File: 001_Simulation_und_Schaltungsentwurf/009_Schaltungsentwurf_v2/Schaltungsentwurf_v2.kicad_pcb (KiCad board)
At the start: 4 copper layers, 146 x 82.1 mm, 101 parts, among them IC1 MPY634KP, IC2 MPY634KP, IC3 MPY634KP, J1 Screw_Terminal_01x04, J2 Conn_Coaxial, J3 Conn_Coaxial, J4 Conn_Coaxial, J5 Conn_Coaxial, J6 Conn_Coaxial, SW1 SW_MEC_5G, U1 TL082, U2 TL082, U3 MCP4261-104E_P, U4 MCP4261-104E_P, U5 TL082, U6 LM2596T-3.3

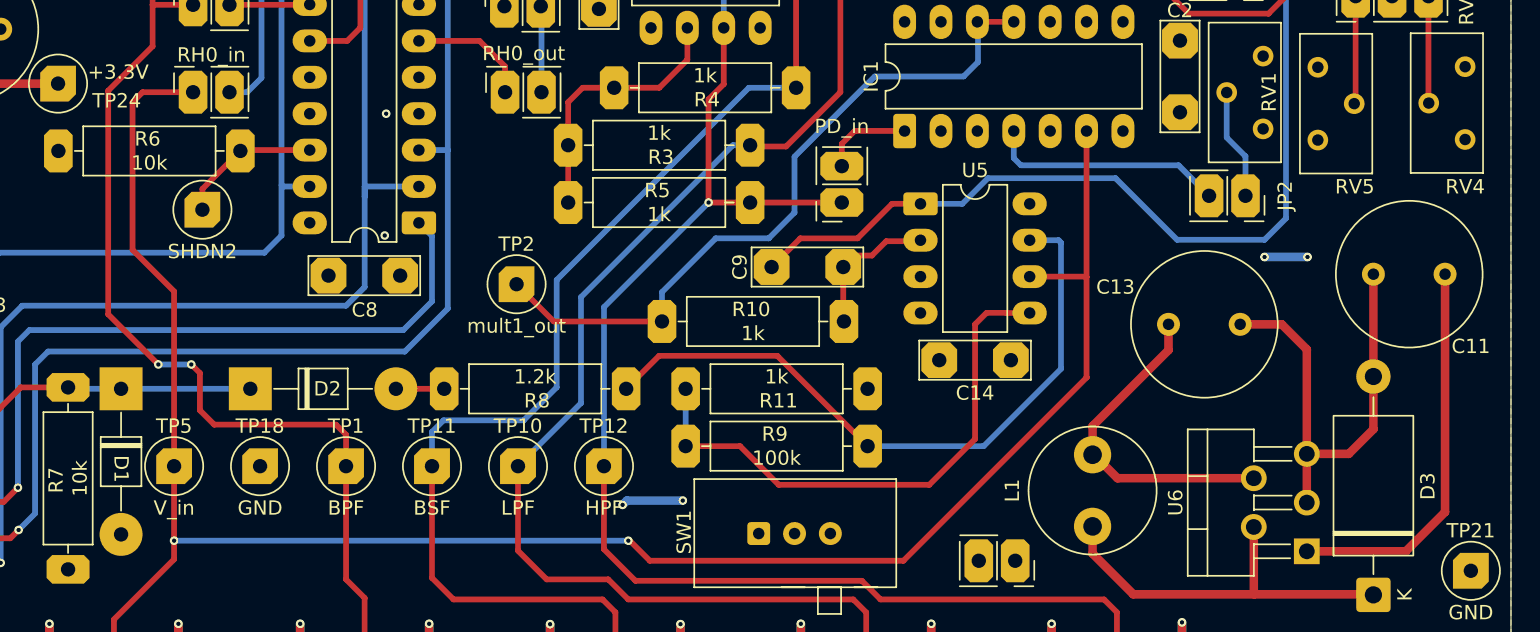
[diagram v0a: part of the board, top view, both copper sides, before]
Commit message: PD-Vermessung und Sprungantwortsimulation
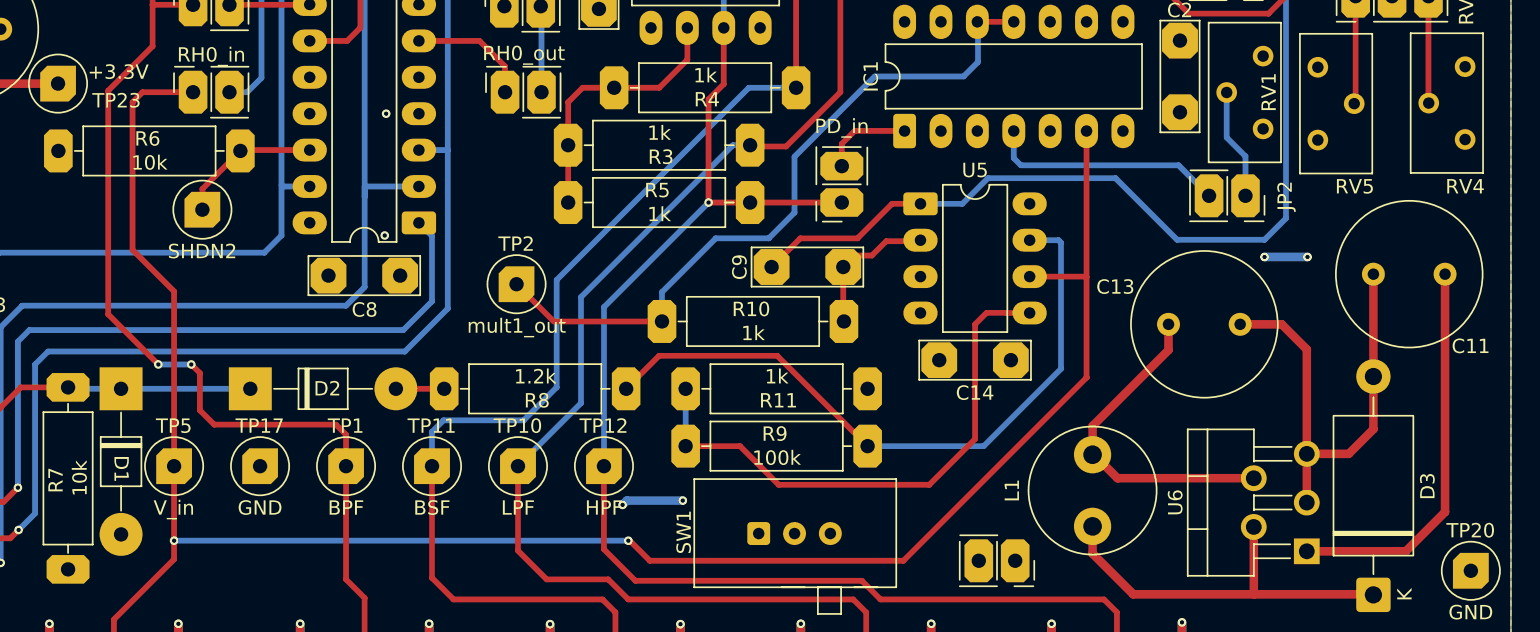
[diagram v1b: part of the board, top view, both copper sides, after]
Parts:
- renumbered JP17 to JP16, JP18 to JP17, JP19 to JP18, TP16 to TP15, TP17 to TP16, TP18 to TP17, TP19 to TP18, TP20 to TP19, TP21 to TP20, TP22 to TP21, TP23 to TP22, TP24 to TP23
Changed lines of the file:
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@@
 	(net 89 "unconnected-(U4-P0B-Pad10)")
 	(net 90 "HPF_in")
-	(net 91 "Net-(JP19-A)")
+	(net 91 "Net-(JP16-A)")
 	(net 92 "Net-(D1-K)")
 	(net 93 "Net-(D2-A)")
@@
 	(net 95 "Net-(JP17-A)")
 	(net 96 "Net-(JP18-A)")
-	(net 97 "Net-(JP19-B)")
+	(net 97 "Net-(JP18-B)")
 	(net 98 "Net-(R8-Pad1)")
 	(footprint "000_OUF:TestPoint"
@@
 				(keep_text_aligned yes)
 			)
-			(gr_text "0,1673 in"
+			(gr_text "4,2500 mm"
 				(at 189.775 123.55 0)
 				(layer "User.2")
@@
 				(keep_text_aligned yes)
 			)
-			(gr_text "0,1673 in"
+			(gr_text "4,2500 mm"
 				(at 194.025 123.548 0)
 				(layer "User.2")
@@
 		(descr "THT pad as test Point, diameter 2.0mm, hole diameter 1.0mm")
 		(tags "test point THT pad")
-		(property "Reference" "TP23"
+		(property "Reference" "TP22"
 			(at -12.2682 -3.9878 0)
 			(layer "F.SilkS")
@@
 		(descr "THT pad as test Point, diameter 2.0mm, hole diameter 1.0mm")
 		(tags "test point THT pad")
-		(property "Reference" "TP24"
+		(property "Reference" "TP23"
 			(at -12.2682 -3.9878 0)
 			(layer "F.SilkS")
@@
 		(descr "Through hole straight socket strip, 1x02, 2.54mm pitch, single row (from Kicad 4.0.7), script generated")
 		(tags "Through hole socket strip THT 1x02 2.54mm single row")
-		(property "Reference" "JP19"
+		(property "Reference" "JP18"
 			(at 0 -2.77 90)
 			(layer "F.SilkS")
@@
 			(chamfer_ratio 0.2)
 			(chamfer top_left top_right bottom_left bottom_right)
-			(net 91 "Net-(JP19-A)")
+			(net 96 "Net-(JP18-A)")
 			(pinfunction "A")
 			(pintype "passive")
@@
 			(chamfer_ratio 0.2)
 			(chamfer top_left top_right bottom_left bottom_right)
-			(net 97 "Net-(JP19-B)")
+			(net 97 "Net-(JP18-B)")
 			(pinfunction "B")
 			(pintype "passive")
@@
 		(descr "Through hole straight socket strip, 1x02, 2.54mm pitch, single row (from Kicad 4.0.7), script generated")
 		(tags "Through hole socket strip THT 1x02 2.54mm single row")
-		(property "Reference" "JP18"
+		(property "Reference" "JP17"
 			(at 0 -2.77 90)
 			(layer "F.SilkS")
@@
 			(chamfer_ratio 0.2)
 			(chamfer top_left top_right bottom_left bottom_right)
-			(net 96 "Net-(JP18-A)")
+			(net 95 "Net-(JP17-A)")
 			(pinfunction "A")
 			(pintype "passive")
@@
 			(layers "*.Cu" "*.Mask")
 			(remove_unused_layers no)
-			(net 95 "Net-(JP17-A)")
+			(net 91 "Net-(JP16-A)")
 			(pinfunction "1")
 			(pintype "passive")
@@
 				(font
 					(size 1 1)
-					(thickness 0.1)
+					(thickness 0.15)
 				)
 			)
@@
 				(keep_text_aligned yes)
 			)
-			(gr_text "0,1673 in"
+			(gr_text "4,2500 mm"
 				(at 124.025 123.548 0)
 				(layer "User.2")
@@
 				(keep_text_aligned yes)
 			)
-			(gr_text "0,1673 in"
+			(gr_text "4,2500 mm"
 				(at 119.775 123.55 0)
 				(layer "User.2")
@@
 				(keep_text_aligned yes)
 			)
-			(gr_text "0,1673 in"
+			(gr_text "4,2500 mm"
 				(at 137.275 123.55 0)
 				(layer "User.2")
@@
 				(keep_text_aligned yes)
 			)
-			(gr_text "0,1673 in"
+			(gr_text "4,2500 mm"
 				(at 141.525 123.548 0)
 				(layer "User.2")
@@
 		(descr "THT pad as test Point, diameter 2.0mm, hole diameter 1.0mm")
 		(tags "test point THT pad")
-		(property "Reference" "TP21"
+		(property "Reference" "TP20"
 			(at -12.2682 -3.9878 0)
 			(layer "F.SilkS")
@@
 			(layers "*.Cu" "*.Mask")
 			(remove_unused_layers no)
-			(net 91 "Net-(JP19-A)")
+			(net 96 "Net-(JP18-A)")
 			(pinfunction "FB")
 			(pintype "input")
@@
 			(layers "*.Cu" "*.Mask")
 			(remove_unused_layers no)
-			(net 91 "Net-(JP19-A)")
+			(net 96 "Net-(JP18-A)")
 			(pintype "passive")
 		)
@@
 		(descr "Through hole straight socket strip, 1x02, 2.54mm pitch, single row (from Kicad 4.0.7), script generated")
 		(tags "Through hole socket strip THT 1x02 2.54mm single row")
-		(property "Reference" "JP17"
+		(property "Reference" "JP16"
 			(at 0 -2.77 90)
 			(layer "F.SilkS")
@@
 			(chamfer_ratio 0.2)
 			(chamfer top_left top_right bottom_left bottom_right)
-			(net 95 "Net-(JP17-A)")
+			(net 91 "Net-(JP16-A)")
 			(pinfunction "A")
 			(pintype "passive")
@@
 			(layers "*.Cu" "*.Mask")
 			(remove_unused_layers no)
-			(net 96 "Net-(JP18-A)")
+			(net 95 "Net-(JP17-A)")
 			(pinfunction "1")
 			(pintype "passive")
@@
 		(descr "THT pad as test Point, diameter 2.0mm, hole diameter 1.0mm")
 		(tags "test point THT pad")
-		(property "Reference" "TP17"
+		(property "Reference" "TP16"
 			(at -12.2682 -3.9878 0)
 			(layer "F.SilkS")
@@
 		(descr "THT pad as test Point, diameter 2.0mm, hole diameter 1.0mm")
 		(tags "test point THT pad")
-		(property "Reference" "TP18"
+		(property "Reference" "TP17"
 			(at -12.2682 -3.9878 0)
 			(layer "F.SilkS")
@@
 		(descr "THT pad as test Point, diameter 2.0mm, hole diameter 1.0mm")
 		(tags "test point THT pad")
-		(property "Reference" "TP22"
+		(property "Reference" "TP21"
 			(at -12.2682 -3.9878 0)
 			(layer "F.SilkS")
@@
 				(keep_text_aligned yes)
 			)
-			(gr_text "0,1673 in"
+			(gr_text "4,2500 mm"
 				(at 176.525 123.548 0)
 				(layer "User.2")
@@
 				(keep_text_aligned yes)
 			)
-			(gr_text "0,1673 in"
+			(gr_text "4,2500 mm"
 				(at 172.275 123.55 0)
 				(layer "User.2")
@@
 		(descr "THT pad as test Point, diameter 2.0mm, hole diameter 1.0mm")
 		(tags "test point THT pad")
-		(property "Reference" "TP16"
+		(property "Reference" "TP15"
 			(at -12.2682 -3.9878 0)
 			(layer "F.SilkS")
@@
 				(font
 					(size 1 1)
-					(thickness 0.1)
+					(thickness 0.15)
 				)
 			)
@@
 		(descr "THT pad as test Point, diameter 2.0mm, hole diameter 1.0mm")
 		(tags "test point THT pad")
-		(property "Reference" "TP19"
+		(property "Reference" "TP18"
 			(at -12.2682 -3.9878 0)
 			(layer "F.SilkS")
@@
 			(layers "*.Cu" "*.Mask")
 			(remove_unused_layers no)
-			(net 91 "Net-(JP19-A)")
+			(net 96 "Net-(JP18-A)")
 			(pintype "passive")
 		)
@@
 				(keep_text_aligned yes)
 			)
-			(gr_text "0,1673 in"
+			(gr_text "4,2500 mm"
 				(at 154.775 123.575 0)
 				(layer "User.2")
@@
 				(keep_text_aligned yes)
 			)
-			(gr_text "0,1673 in"
+			(gr_text "4,2500 mm"
 				(at 159.025 123.573 0)
 				(layer "User.2")
@@
 		(descr "THT pad as test Point, diameter 2.0mm, hole diameter 1.0mm")
 		(tags "test point THT pad")
-		(property "Reference" "TP20"
+		(property "Reference" "TP19"
 			(at -12.2682 -3.9878 0)
 			(layer "F.SilkS")
@@
 			(layers "*.Cu" "*.Mask")
 			(remove_unused_layers no)
-			(net 97 "Net-(JP19-B)")
+			(net 97 "Net-(JP18-B)")
 			(pinfunction "A")
 			(pintype "passive")
@@
 			(layers "*.Cu" "*.Mask")
 			(remove_unused_layers no)
-			(net 97 "Net-(JP19-B)")
+			(net 97 "Net-(JP18-B)")
 			(pinfunction "A")
 			(pintype "passive")
@@
 			(keep_text_aligned yes)
 		)
-		(gr_text "0,1969"
+		(gr_text "5"
 			(at 130.3 135.1 0)
 			(layer "User.2")
@@
 			(keep_text_aligned yes)
 		)
-		(gr_text "0,1969"
+		(gr_text "5"
 			(at 179.1 134.55 0)
 			(layer "User.2")
@@
 			(keep_text_aligned yes)
 		)
-		(gr_text "0,1969"
+		(gr_text "5"
 			(at 146.5 134.65 0)
 			(layer "User.2")
@@
 			(keep_text_aligned yes)
 		)
-		(gr_text "0,2559"
+		(gr_text "6,5"
 			(at 76.65 48.35 0)
 			(layer "User.2")
@@
 			(keep_text_aligned yes)
 		)
-		(gr_text "0,2559"
+		(gr_text "6,5"
 			(at 71.25 53.35 90)
 			(layer "User.2")
@@
 			(keep_text_aligned yes)
 		)
-		(gr_text "0,1969"
+		(gr_text "5"
 			(at 162.8 134.55 0)
 			(layer "User.2")
@@
 	)
 	(segment
-		(start 190.2 114.2)
-		(end 190.2 112.3)
-		(width 0.6)
-		(layer "F.Cu")
-		(net 91)
-	)
-	(segment
-		(start 195.5 107)
-		(end 195.5 105.2)
-		(width 0.6)
-		(layer "F.Cu")
-		(net 91)
-	)
-	(segment
-		(start 190.2 112.3)
-		(end 195.5 107)
-		(width 0.6)
-		(layer "F.Cu")
-		(net 91)
-	)
-	(segment
-		(start 201.45 115.94)
-		(end 191.94 115.94)
-		(width 0.6)
+		(start 207.12 64.66)
+		(end 207.12 60.27)
+		(width 0.4)
 		(layer "F.Cu")
 		(net 91)
 	)
 	(segment
-		(start 191.94 115.94)
-		(end 190.2 114.2)
-		(width 0.6)
+		(start 207.12 60.27)
+		(end 207.05 60.2)
+		(width 0.4)
 		(layer "F.Cu")
 		(net 91)
 	)
 	(segment
-		(start 188.3 114.3)
-		(end 190.2 114.3)
-		(width 0.6)
-		(layer "In2.Cu")
-		(net 91)
-	)
-	(segment
-		(start 184.8 121.7)
-		(end 184.8 117.8)
-		(width 0.6)
-		(layer "In2.Cu")
-		(net 91)
-	)
-	(segment
-		(start 184.8 117.8)
-		(end 188.3 114.3)
-		(width 0.6)
-		(layer "In2.Cu")
-		(net 91)
-	)
-	(segment
 		(start 118.7 109.6)
 		(end 115.4 109.6)
@@
 	)
 	(segment
-		(start 207.12 64.66)
-		(end 207.12 60.27)
+		(start 214.12 64.56)
+		(end 216.75 61.93)
 		(width 0.4)
 		(layer "F.Cu")
@@
 	)
 	(segment
-		(start 207.12 60.27)
-		(end 207.05 60.2)
+		(start 216.75 61.93)
+		(end 216.75 60.2)
 		(width 0.4)
 		(layer "F.Cu")
@@
 	)
 	(segment
-		(start 214.12 64.56)
-		(end 216.75 61.93)
-		(width 0.4)
+		(start 190.2 114.2)
+		(end 190.2 112.3)
+		(width 0.6)
 		(layer "F.Cu")
 		(net 96)
 	)
 	(segment
-		(start 216.75 61.93)
-		(end 216.75 60.2)
-		(width 0.4)
+		(start 195.5 107)
+		(end 195.5 105.2)
+		(width 0.6)
 		(layer "F.Cu")
 		(net 96)
 	)
+	(segment
+		(start 190.2 112.3)
+		(end 195.5 107)
+		(width 0.6)
+		(layer "F.Cu")
+		(net 96)
+	)
+	(segment
+		(start 201.45 115.94)
+		(end 191.94 115.94)
+		(width 0.6)
+		(layer "F.Cu")
+		(net 96)
+	)
+	(segment
+		(start 191.94 115.94)
+		(end 190.2 114.2)
+		(width 0.6)
+		(layer "F.Cu")
+		(net 96)
+	)
+	(segment
+		(start 188.3 114.3)
+		(end 190.2 114.3)
+		(width 0.6)
+		(layer "In2.Cu")
+		(net 96)
+	)
+	(segment
+		(start 184.8 121.7)
+		(end 184.8 117.8)
+		(width 0.6)
+		(layer "In2.Cu")
+		(net 96)
+	)
+	(segment
+		(start 184.8 117.8)
+		(end 188.3 114.3)
+		(width 0.6)
+		(layer "In2.Cu")
+		(net 96)
+	)
